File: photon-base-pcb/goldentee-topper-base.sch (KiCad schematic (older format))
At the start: 79 parts, among them M1 photon_module, P1 CONN_01X04, P2 CONN_01X16, Q1 Q_NMOS_DGS, Q10 Q_PMOS_SDGD, Q11 Q_NMOS_DGS, Q12 Q_PMOS_SDGD, Q13 Q_NMOS_DGS, Q14 Q_PMOS_SDGD, Q2 Q_PMOS_SDGD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

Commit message: first concept layout
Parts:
- removed D1, D2, D3, D4, D5, D6, D7: LED, LEDs:LED_0603, symbol LED
- removed Q10, Q12, Q14, Q2, Q4, Q6, Q8: Q_PMOS_SDGD, TO_SOT_Packages_SMD:SOT-223, symbol Q_PMOS_SDGD
- removed R10, R11, R13, R14, R15, R16, R9: 47K, Resistors_SMD:R_0603_HandSoldering, symbol R_Small
- removed R17, R2, R25, R27, R4, R6, R8: 4.7K, Resistors_SMD:R_0603_HandSoldering, symbol R_Small
- added Q10, Q12, Q14, Q2, Q4, Q6, Q8: Q_PMOS_GDS, TO_SOT_Packages_SMD:TO-252-2Lead, symbol Q_PMOS_GDS
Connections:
- wire segments 162 -> 140

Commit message: Small Square pcb, silk yet to be arranged.
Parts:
- removed C5, C6: 10uF 25V, Capacitors_SMD:C_1210_HandSoldering, symbol C_Small
- removed R28: 47K, Resistors_SMD:R_0603_HandSoldering, symbol R_Small
- removed U1: NCP1117ST50T3G, TO_SOT_Packages_SMD:SOT-223, symbol NCP1117ST50T3G
- removed U3: NCP1117ST33T3G, TO_SOT_Packages_SMD:SOT-223, symbol NCP1117ST33T3G
- added R2: 47K, Resistors_SMD:R_0603_HandSoldering, symbol R_Small
- added U1: NCP1117, TO_SOT_Packages_SMD:SOT-223, symbol NCP1117
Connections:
- net labels added: BOTTOM_CLK_3V3, LED_GND, LED_PWR, TOP_CLK_3V3
- net labels removed: LED_CLK_3V3
- wire segments 140 -> 138
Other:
- moved on the sheet: R40

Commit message: V3 Release
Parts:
- added P3: CONN_01X06, Pin_Headers:Pin_Header_Straight_1x06_Pitch2.54mm, symbol CONN_01X06
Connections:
- net labels added: UART_RXD, UART_TXD
- wire segments 138 -> 142
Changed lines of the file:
@@
 	2100 1300 2100 1200
 Connection ~ 2100 1200
+$Comp
+L CONN_01X06 P3
+U 1 1 58BF8C75
+P 5300 5000
+F 0 "P3" H 5300 5350 50  0000 C CNN
+F 1 "CONN_01X06" V 5400 5000 50  0000 C CNN
+F 2 "Pin_Headers:Pin_Header_Straight_1x06_Pitch2.54mm" H 5300 5000 50  0001 C CNN
+F 3 "" H 5300 5000 50  0000 C CNN
+	1    5300 5000
+	1    0    0    -1
+$EndComp
+$Comp
+L GND #PWR037
+U 1 1 58BF8D84
+P 5100 4750
+F 0 "#PWR037" H 5100 4500 50  0001 C CNN
+F 1 "GND" V 5100 4500 50  0000 C CNN
+F 2 "" H 5100 4750 50  0000 C CNN
+F 3 "" H 5100 4750 50  0000 C CNN
+	1    5100 4750
+	0    1    1    0
+$EndComp
+Wire Wire Line
+	3250 6250 2250 6250
+Wire Wire Line
+	3250 6150 2250 6150
+Wire Wire Line
+	5100 5050 4300 5050
+Wire Wire Line
+	5100 5150 4300 5150
+Text Label 4300 5150 0    60   ~ 0
+UART_RXD
+Text Label 4300 5050 0    60   ~ 0
+UART_TXD
+Text Label 2250 6150 0    60   ~ 0
+UART_RXD
+Text Label 2250 6250 0    60   ~ 0
+UART_TXD
 $EndSCHEMATC

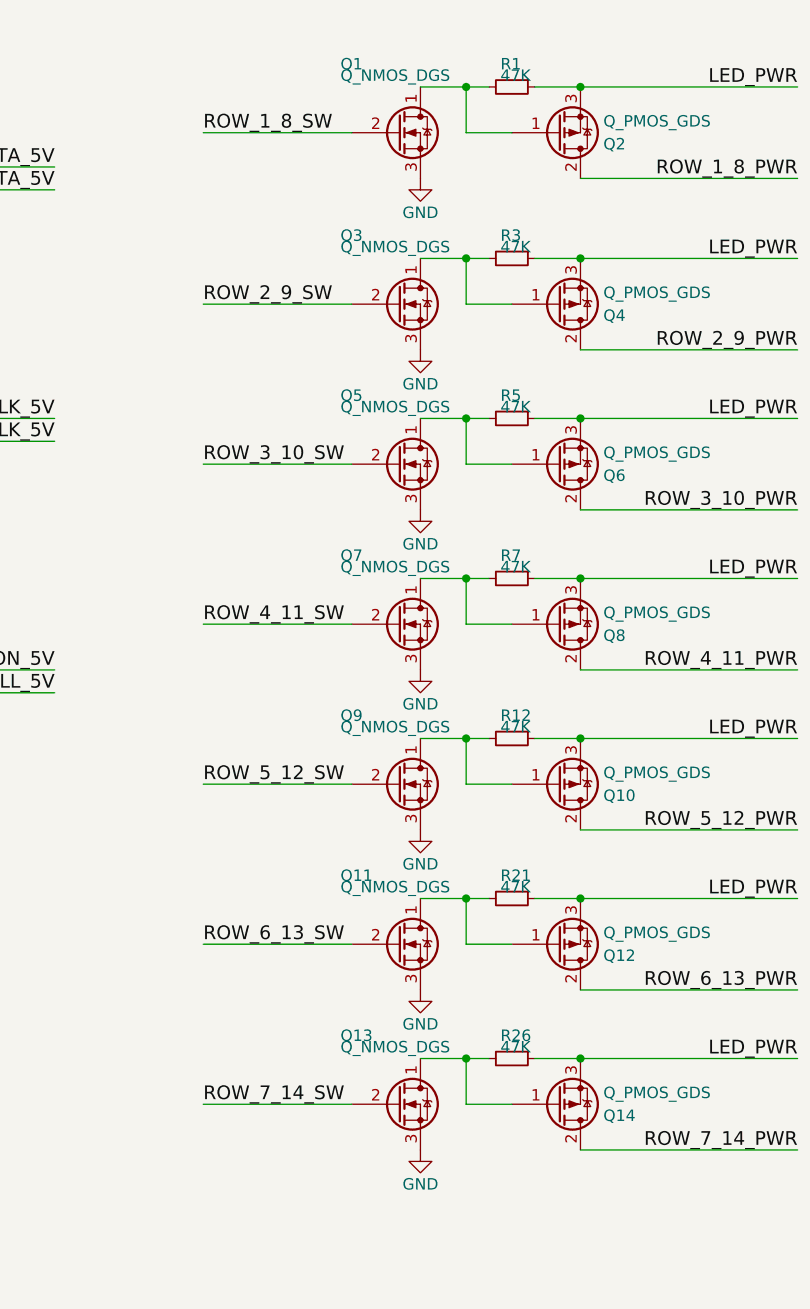
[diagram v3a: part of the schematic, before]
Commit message: fixed sideways nfets, relayed out the area around the new FET configuration. BOM updates for all the initial parts.  BOM reflects the fixed NFET pinout.
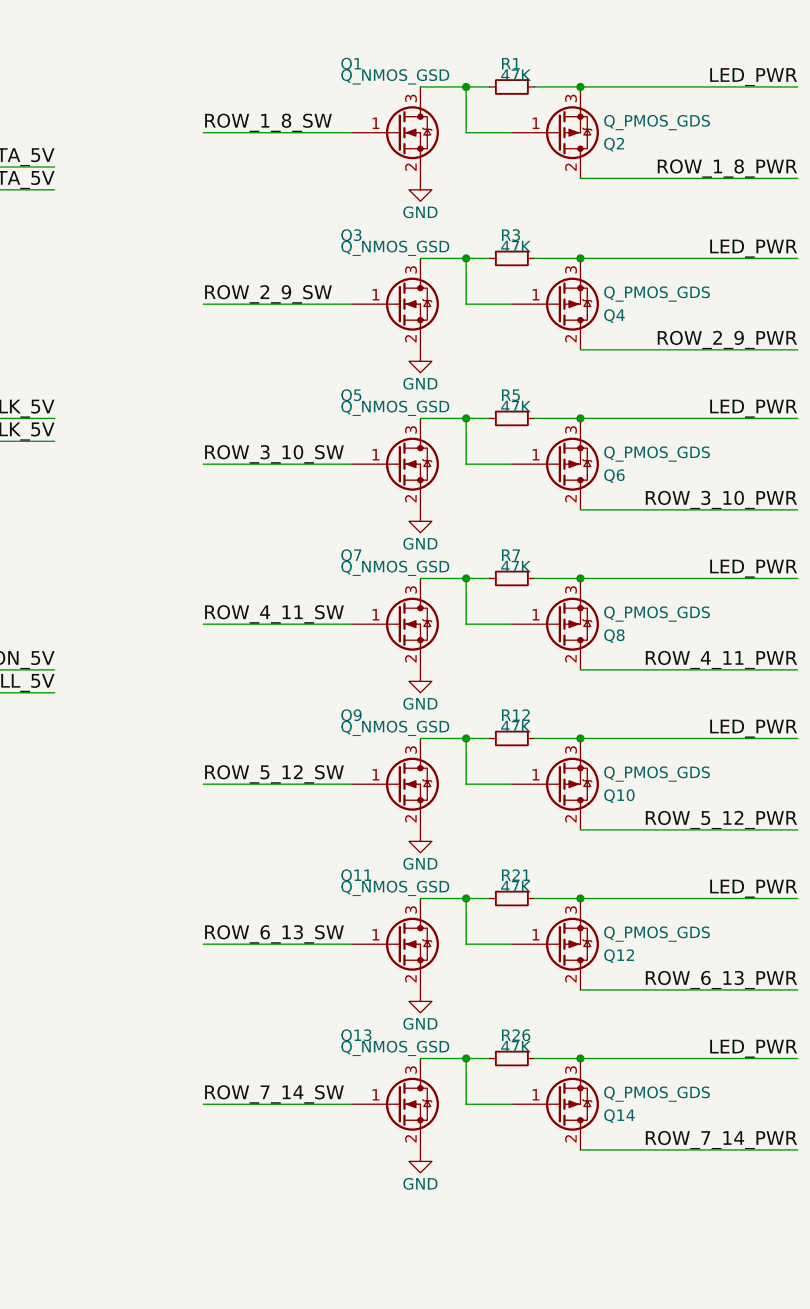
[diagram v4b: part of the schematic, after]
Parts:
- removed Q1, Q11, Q13, Q3, Q5, Q7, Q9: Q_NMOS_DGS, TO_SOT_Packages_SMD:SOT-23_Handsoldering, symbol Q_NMOS_DGS
- added Q1, Q11, Q13, Q3, Q5, Q7, Q9: Q_NMOS_GSD, TO_SOT_Packages_SMD:SOT-23_Handsoldering, symbol Q_NMOS_GSD
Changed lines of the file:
@@
 	4450 1550 3650 1550
-$Comp
-L Q_NMOS_DGS Q1
-U 1 1 58BEC22C
-P 7900 1400
-F 0 "Q1" H 7650 1700 50  0000 L CNN
-F 1 "Q_NMOS_DGS" H 7650 1650 50  0000 L CNN
-F 2 "TO_SOT_Packages_SMD:SOT-23_Handsoldering" H 8100 1500 50  0001 C CNN
-F 3 "" H 7900 1400 50  0000 C CNN
-	1    7900 1400
-	1    0    0    -1
-$EndComp
 $Comp
 L GND #PWR027
@@
 	0    1    1    0
 $EndComp
-$Comp
-L Q_NMOS_DGS Q5
-U 1 1 58BEE5A5
-P 7900 2850
-F 0 "Q5" H 7650 3150 50  0000 L CNN
-F 1 "Q_NMOS_DGS" H 7650 3100 50  0000 L CNN
-F 2 "TO_SOT_Packages_SMD:SOT-23_Handsoldering" H 8100 2950 50  0001 C CNN
-F 3 "" H 7900 2850 50  0000 C CNN
-	1    7900 2850
-	1    0    0    -1
-$EndComp
 Text Label 7050 2850 0    60   ~ 0
 ROW_3_10_SW
@@
 	0    1    1    0
 $EndComp
-$Comp
-L Q_NMOS_DGS Q3
-U 1 1 58BEFCF6
-P 7900 2150
-F 0 "Q3" H 7650 2450 50  0000 L CNN
-F 1 "Q_NMOS_DGS" H 7650 2400 50  0000 L CNN
-F 2 "TO_SOT_Packages_SMD:SOT-23_Handsoldering" H 8100 2250 50  0001 C CNN
-F 3 "" H 7900 2150 50  0000 C CNN
-	1    7900 2150
-	1    0    0    -1
-$EndComp
 Text Label 7050 2150 0    60   ~ 0
 ROW_2_9_SW
@@
 	0    1    1    0
 $EndComp
-$Comp
-L Q_NMOS_DGS Q7
-U 1 1 58BEFDA6
-P 7900 3550
-F 0 "Q7" H 7650 3850 50  0000 L CNN
-F 1 "Q_NMOS_DGS" H 7650 3800 50  0000 L CNN
-F 2 "TO_SOT_Packages_SMD:SOT-23_Handsoldering" H 8100 3650 50  0001 C CNN
-F 3 "" H 7900 3550 50  0000 C CNN
-	1    7900 3550
-	1    0    0    -1
-$EndComp
 Text Label 7050 3550 0    60   ~ 0
 ROW_4_11_SW
@@
 	0    1    1    0
 $EndComp
-$Comp
-L Q_NMOS_DGS Q9
-U 1 1 58BEFED6
-P 7900 4250
-F 0 "Q9" H 7650 4550 50  0000 L CNN
-F 1 "Q_NMOS_DGS" H 7650 4500 50  0000 L CNN
-F 2 "TO_SOT_Packages_SMD:SOT-23_Handsoldering" H 8100 4350 50  0001 C CNN
-F 3 "" H 7900 4250 50  0000 C CNN
-	1    7900 4250
-	1    0    0    -1
-$EndComp
 Text Label 7050 4250 0    60   ~ 0
 ROW_5_12_SW
@@
 	0    1    1    0
 $EndComp
-$Comp
-L Q_NMOS_DGS Q11
-U 1 1 58BEFF7A
-P 7900 4950
-F 0 "Q11" H 7650 5250 50  0000 L CNN
-F 1 "Q_NMOS_DGS" H 7650 5200 50  0000 L CNN
-F 2 "TO_SOT_Packages_SMD:SOT-23_Handsoldering" H 8100 5050 50  0001 C CNN
-F 3 "" H 7900 4950 50  0000 C CNN
-	1    7900 4950
-	1    0    0    -1
-$EndComp
 Text Label 7050 4950 0    60   ~ 0
 ROW_6_13_SW
@@
 	1    8400 5450
 	0    1    1    0
-$EndComp
-$Comp
-L Q_NMOS_DGS Q13
-U 1 1 58BF004E
-P 7900 5650
-F 0 "Q13" H 7650 5950 50  0000 L CNN
-F 1 "Q_NMOS_DGS" H 7650 5900 50  0000 L CNN
-F 2 "TO_SOT_Packages_SMD:SOT-23_Handsoldering" H 8100 5750 50  0001 C CNN
-F 3 "" H 7900 5650 50  0000 C CNN
-	1    7900 5650
-	1    0    0    -1
 $EndComp
 Text Label 7050 5650 0    60   ~ 0
@@
 Text Label 2250 6250 0    60   ~ 0
 UART_TXD
+$Comp
+L Q_NMOS_GSD Q1
+U 1 1 58C1F2CD
+P 7900 1400
+F 0 "Q1" H 7650 1700 50  0000 L CNN
+F 1 "Q_NMOS_GSD" H 7650 1650 50  0000 L CNN
+F 2 "TO_SOT_Packages_SMD:SOT-23_Handsoldering" H 8100 1500 50  0001 C CNN
+F 3 "" H 7900 1400 50  0000 C CNN
+	1    7900 1400
+	1    0    0    -1
+$EndComp
+$Comp
+L Q_NMOS_GSD Q3
+U 1 1 58C2035C
+P 7900 2150
+F 0 "Q3" H 7650 2450 50  0000 L CNN
+F 1 "Q_NMOS_GSD" H 7650 2400 50  0000 L CNN
+F 2 "TO_SOT_Packages_SMD:SOT-23_Handsoldering" H 8100 2250 50  0001 C CNN
+F 3 "" H 7900 2150 50  0000 C CNN
+	1    7900 2150
+	1    0    0    -1
+$EndComp
+$Comp
+L Q_NMOS_GSD Q5
+U 1 1 58C20EFC
+P 7900 2850
+F 0 "Q5" H 7650 3150 50  0000 L CNN
+F 1 "Q_NMOS_GSD" H 7650 3100 50  0000 L CNN
+F 2 "TO_SOT_Packages_SMD:SOT-23_Handsoldering" H 8100 2950 50  0001 C CNN
+F 3 "" H 7900 2850 50  0000 C CNN
+	1    7900 2850
+	1    0    0    -1
+$EndComp
+$Comp
+L Q_NMOS_GSD Q7
+U 1 1 58C20FB6
+P 7900 3550
+F 0 "Q7" H 7650 3850 50  0000 L CNN
+F 1 "Q_NMOS_GSD" H 7650 3800 50  0000 L CNN
+F 2 "TO_SOT_Packages_SMD:SOT-23_Handsoldering" H 8100 3650 50  0001 C CNN
+F 3 "" H 7900 3550 50  0000 C CNN
+	1    7900 3550
+	1    0    0    -1
+$EndComp
+$Comp
+L Q_NMOS_GSD Q9
+U 1 1 58C2106E
+P 7900 4250
+F 0 "Q9" H 7650 4550 50  0000 L CNN
+F 1 "Q_NMOS_GSD" H 7650 4500 50  0000 L CNN
+F 2 "TO_SOT_Packages_SMD:SOT-23_Handsoldering" H 8100 4350 50  0001 C CNN
+F 3 "" H 7900 4250 50  0000 C CNN
+	1    7900 4250
+	1    0    0    -1
+$EndComp
+$Comp
+L Q_NMOS_GSD Q11
+U 1 1 58C2112A
+P 7900 4950
+F 0 "Q11" H 7650 5250 50  0000 L CNN
+F 1 "Q_NMOS_GSD" H 7650 5200 50  0000 L CNN
+F 2 "TO_SOT_Packages_SMD:SOT-23_Handsoldering" H 8100 5050 50  0001 C CNN
+F 3 "" H 7900 4950 50  0000 C CNN
+	1    7900 4950
+	1    0    0    -1
+$EndComp
+$Comp
+L Q_NMOS_GSD Q13
+U 1 1 58C21290
+P 7900 5650
+F 0 "Q13" H 7650 5950 50  0000 L CNN
+F 1 "Q_NMOS_GSD" H 7650 5900 50  0000 L CNN
+F 2 "TO_SOT_Packages_SMD:SOT-23_Handsoldering" H 8100 5750 50  0001 C CNN
+F 3 "" H 7900 5650 50  0000 C CNN
+	1    7900 5650
+	1    0    0    -1
+$EndComp
 $EndSCHEMATC

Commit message: level shifter footprint update
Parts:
- U2, U4, U5: footprint SMD_Packages:SOIC-8-N -> goldentee_topper_base:SN74LVC2T45DCTR
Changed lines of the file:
@@
 F 0 "U2" H 4700 2400 60  0000 C CNN
 F 1 "SN74LVC2T45" H 4950 1800 60  0000 C CNN
-F 2 "SMD_Packages:SOIC-8-N" H 5150 1850 60  0001 C CNN
+F 2 "goldentee_topper_base:SN74LVC2T45DCTR" H 5150 1850 60  0001 C CNN
 F 3 "" H 5150 1850 60  0001 C CNN
 	1    5050 1850
@@
 F 0 "U4" H 4700 3500 60  0000 C CNN
 F 1 "SN74LVC2T45" H 4950 2900 60  0000 C CNN
-F 2 "SMD_Packages:SOIC-8-N" H 5150 2950 60  0001 C CNN
+F 2 "goldentee_topper_base:SN74LVC2T45DCTR" H 5150 2950 60  0001 C CNN
 F 3 "" H 5150 2950 60  0001 C CNN
 	1    5050 2950
@@
 F 0 "U5" H 4700 4600 60  0000 C CNN
 F 1 "SN74LVC2T45" H 4950 4000 60  0000 C CNN
-F 2 "SMD_Packages:SOIC-8-N" H 5150 4050 60  0001 C CNN
+F 2 "goldentee_topper_base:SN74LVC2T45DCTR" H 5150 4050 60  0001 C CNN
 F 3 "" H 5150 4050 60  0001 C CNN
 	1    5050 4050
